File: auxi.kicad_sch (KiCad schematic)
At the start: 47 parts

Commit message: feat(pcb): Add design settings, update schematic notes, and modify MP1584 module footprint
- Introduced comprehensive design settings in `auxi.kicad_pro` for improved PCB layout control, including defaults for various design elements and DRC rules.
- Updated schematic notes in `auxi.kicad_sch` to reflect changes in battery connector specifications and additional circuit details.
- Enhanced the MP1584 module footprint in `MP1584_Mini_PROVISIONAL.kicad_mod` with corrected dimensions, improved pad layout, and updated silk screen labels for clarity.
- Added a new PCB placement image `auxi_pcb_placement.png` to the documentation for better assembly guidance.
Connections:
- net GND: now also J_BAT1.1 (Pin_1); no longer J_BAT1.2 (Pin_2)
- net SW_BAT: now also J_BAT1.2 (Pin_2); no longer J_BAT1.1 (Pin_1)
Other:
- note added: "J_BAT1 (XT30UPB-M): pin 1 = BAT- (lado biselado), pin 2 = BAT+ (lado plano). J_SWITCH1: interruptor externo. Por aqui pasa TODA la corriente del robot: bornera 5.08 mm y cable 20 AWG, nunca Dupont. R1 1.5k: LED azul a 2.0 mA (6.0 V) - 3.6 mA (8.4 V). Calibrar el MP1584 a 5.0 V con multimetro ANTES de enchufar cualquier modulo. D1 (Schottky): evita que el USB del PC alimente el robot y viceversa. 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"
- note removed: "J_BAT1 (XT30): pin 1 = BAT+, pin 2 = BAT-. J_SWITCH1: interruptor externo. Por aqui pasa TODA la corriente del robot: bornera 5.08 mm y cable 20 AWG, nunca Dupont. R1 1.5k: LED azul a 2.0 mA (6.0 V) - 3.6 mA (8.4 V). Calibrar el MP1584 a 5.0 V con multimetro ANTES de enchufar cualquier modulo. D1 (Schottky): evita que el USB del PC alimente el robot y viceversa. PWR_FLAG: +VBAT_SW, GND y +5V_ESP 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"
- moved on the sheet: J_BAT1
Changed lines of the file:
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@@
 	(label "LED_POWER_A" (at 109.22 284.48 0) (effects (font (size 1.27 1.27)) (justify left bottom)))
 	(text "1. ALIMENTACION: bateria 2S, interruptor, LED de funcionamiento, MP1584, diodo" (exclude_from_sim no) (at 20 240 0) (effects (font (size 3 3) (bold yes)) (justify left bottom)))
-	(text "J_BAT1 (XT30): pin 1 = BAT+, pin 2 = BAT-.\nJ_SWITCH1: interruptor externo. Por aqui pasa TODA la corriente del robot:\nbornera 5.08 mm y cable 20 AWG, nunca Dupont.\nR1 1.5k: LED azul a 2.0 mA (6.0 V) - 3.6 mA (8.4 V).\nCalibrar el MP1584 a 5.0 V con multimetro ANTES de enchufar cualquier modulo.\nD1 (Schottky): evita que el USB del PC alimente el robot y viceversa.\nPWR_FLAG: +VBAT_SW, GND y +5V_ESP solo reciben corriente a traves de\nconectores o del diodo (pines pasivos); las banderas le indican al ERC\nque esas redes SI estan alimentadas." (exclude_from_sim no) (at 20 320 0) (effects (font (size 1.5 1.5)) (justify left bottom)))
+	(text "J_BAT1 (XT30UPB-M): pin 1 = BAT- (lado biselado), pin 2 = BAT+ (lado plano).\nJ_SWITCH1: interruptor externo. Por aqui pasa TODA la corriente del robot:\nbornera 5.08 mm y cable 20 AWG, nunca Dupont.\nR1 1.5k: LED azul a 2.0 mA (6.0 V) - 3.6 mA (8.4 V).\nCalibrar el MP1584 a 5.0 V con multimetro ANTES de enchufar cualquier modulo.\nD1 (Schottky): evita que el USB del PC alimente el robot y viceversa.\nPWR_FLAG: +VBAT_SW, GND y +5V_ESP solo reciben corriente a traves de\nconectores o del diodo (pines pasivos); las banderas le indican al ERC\nque esas redes SI estan alimentadas." (exclude_from_sim no) (at 20 320 0) (effects (font (size 1.5 1.5)) (justify left bottom)))
 	(text "2. ESP32-S3-DevKitC-1 N16R8" (exclude_from_sim no) (at 250 88 0) (effects (font (size 3 3) (bold yes)) (justify left bottom)))
 	(text "Pinout oficial Espressif v1.1 - VERIFICAR contra el clon comprado.\nNo usar: GPIO0/3/45/46 (arranque), 19/20 (USB), 43/44 (consola),\n35/36/37 (PSRAM octal), 38/48 (LED RGB), 47.\nBluetooth: solo BLE (control Xbox por BLE)." (exclude_from_sim no) (at 255 180 0) (effects (font (size 1.5 1.5)) (justify left bottom)))
@@
 		(instances (project "auxi" (path "/bb7d1f02-099e-4e7c-b03d-f19a0737074b" (reference "#PWR050") (unit 1))))
 	)
-	(symbol (lib_id "Connector_Generic:Conn_01x02") (at 30.48 251.46 0) (mirror y) (unit 1) (body_style 1)
+	(symbol (lib_id "Connector_Generic:Conn_01x02") (at 30.48 254 180) (unit 1) (body_style 1)
 		(exclude_from_sim no) (in_bom yes) (on_board yes) (in_pos_files yes) (dnp no)
 		(property "Reference" "J_BAT1" (at 29.21 247.65 0)

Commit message: Add initial DRC violations report, update BOM with correct footprints, modify schematic for clarity, and add PCB top image
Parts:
- removed R3, R4: 4.7k DNP, Resistor_SMD:R_1206_3216Metric, symbol Device:R
- C10, C13, C15, C17, C19, C2, C21, C4, C6: footprint Capacitor_SMD:C_1206_3216Metric -> Capacitor_THT:C_Disc_D5.0mm_W2.5mm_P5.00mm
- C12, C14, C16, C18, C20, C8: footprint Capacitor_SMD:C_1206_3216Metric -> Capacitor_THT:C_Rect_L7.0mm_W3.5mm_P5.00mm
- R1, R2: footprint Resistor_SMD:R_1206_3216Metric -> Resistor_THT:R_Axial_DIN0207_L6.3mm_D2.5mm_P7.62mm_Horizontal
- R3: renamed from R5; footprint Resistor_SMD:R_1206_3216Metric -> Resistor_THT:R_Axial_DIN0207_L6.3mm_D2.5mm_P7.62mm_Horizontal
- R4: renamed from R6; footprint Resistor_SMD:R_1206_3216Metric -> Resistor_THT:R_Axial_DIN0207_L6.3mm_D2.5mm_P7.62mm_Horizontal
- R5: renamed from R7; footprint Resistor_SMD:R_1206_3216Metric -> Resistor_THT:R_Axial_DIN0207_L6.3mm_D2.5mm_P7.62mm_Horizontal
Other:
- note added: "Orden en los 3 conectores: 1 3V3, 2 GND, 3 SDA, 4 SCL, 5 XSHUT. I2C compartido a 100 kHz, cables de 25 cm o menos. Pull-ups I2C: los GY-530 ya los incluyen. Sin pull-ups extra en la placa. Firmware: todos los XSHUT en bajo, activar uno a uno y asignar 0x30, 0x31, 0x32."
- note removed: "Orden en los 3 conectores: 1 3V3, 2 GND, 3 SDA, 4 SCL, 5 XSHUT. I2C compartido a 100 kHz, cables de 25 cm o menos. R3/R4 4.7k = DNP (no montar) salvo que el analisis de pull-ups del GY-530 lo pida. Firmware: todos los XSHUT en bajo, activar uno a uno y asignar 0x30, 0x31, 0x32."

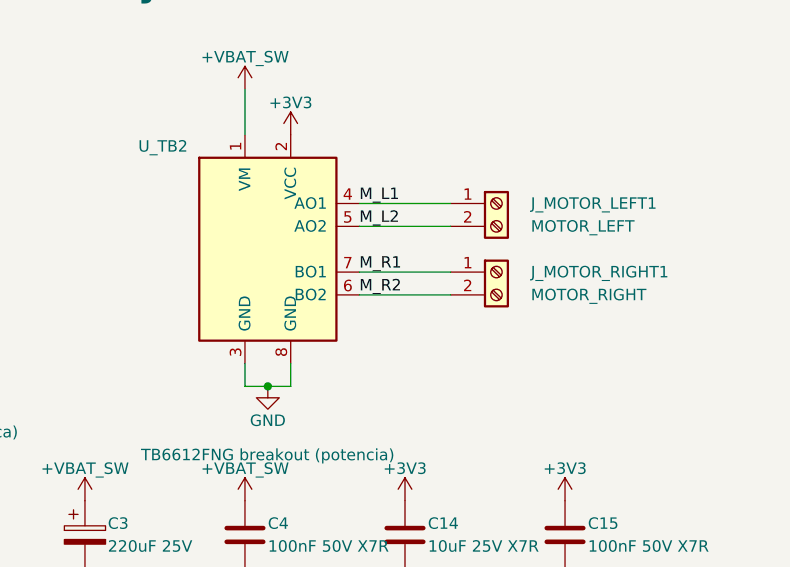
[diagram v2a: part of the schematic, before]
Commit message: Refactor schematic and DRC violation files
- Removed unnecessary wire segments from auxi.kicad_sch to clean up the schematic.
- Added new wire connections to enhance circuit clarity in auxi.kicad_sch.
- Updated timestamp in auxi_drc_violations.json to reflect the latest changes.
- Added a new PDF document (auxi_pcb_real_scale.pdf) containing detailed PCB layouts for both top and bottom layers.
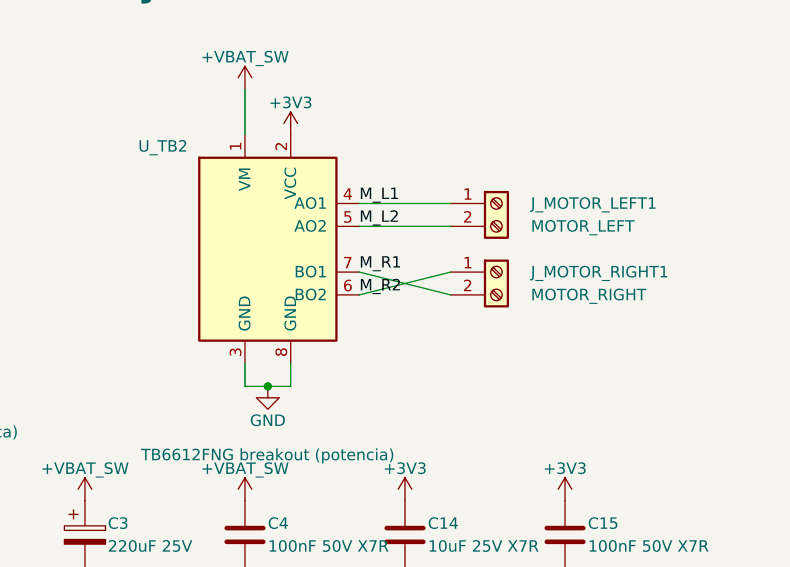
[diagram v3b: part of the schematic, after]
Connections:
- net M_R1: now also J_MOTOR_RIGHT1.2 (Pin_2); no longer J_MOTOR_RIGHT1.1 (Pin_1)
- net M_R2: now also J_MOTOR_RIGHT1.1 (Pin_1); no longer J_MOTOR_RIGHT1.2 (Pin_2)
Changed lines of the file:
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@@
 	(wire
 		(pts
-			(xy 408.94 118.11) (xy 419.1 118.11)
-		)
-		(stroke
-			(width 0)
-			(type default)
-		)
-	)
-	(wire
-		(pts
-			(xy 408.94 120.65) (xy 419.1 120.65)
-		)
-		(stroke
-			(width 0)
-			(type default)
-		)
-	)
-	(wire
-		(pts
 			(xy 165.1 43.18) (xy 170.18 43.18)
 		)
@@
 		)
 	)
+	(wire
+		(pts
+			(xy 408.94 118.11) (xy 419.1 120.65)
+		)
+		(stroke
+			(width 0)
+			(type default)
+		)
+	)
+	(wire
+		(pts
+			(xy 408.94 120.64999999999999) (xy 419.1 118.11)
+		)
+		(stroke
+			(width 0)
+			(type default)
+		)
+	)
